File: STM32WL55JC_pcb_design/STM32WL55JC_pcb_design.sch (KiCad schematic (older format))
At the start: 40 parts, among them J1 Conn_01x03, J10 Conn_01x01_Male, J11 Conn_02x02_Odd_Even, J2 Conn_01x03, J3 Conn_02x05_Odd_Even, J4 Conn_01x03, J5 Conn_01x09, J6 Conn_01x09, J7 Conn_01x03, J8 Conn_01x09, J9 Conn_01x09, U1 STM32WL55JCI7, Y1 32MHz, Y2 32.768kHz

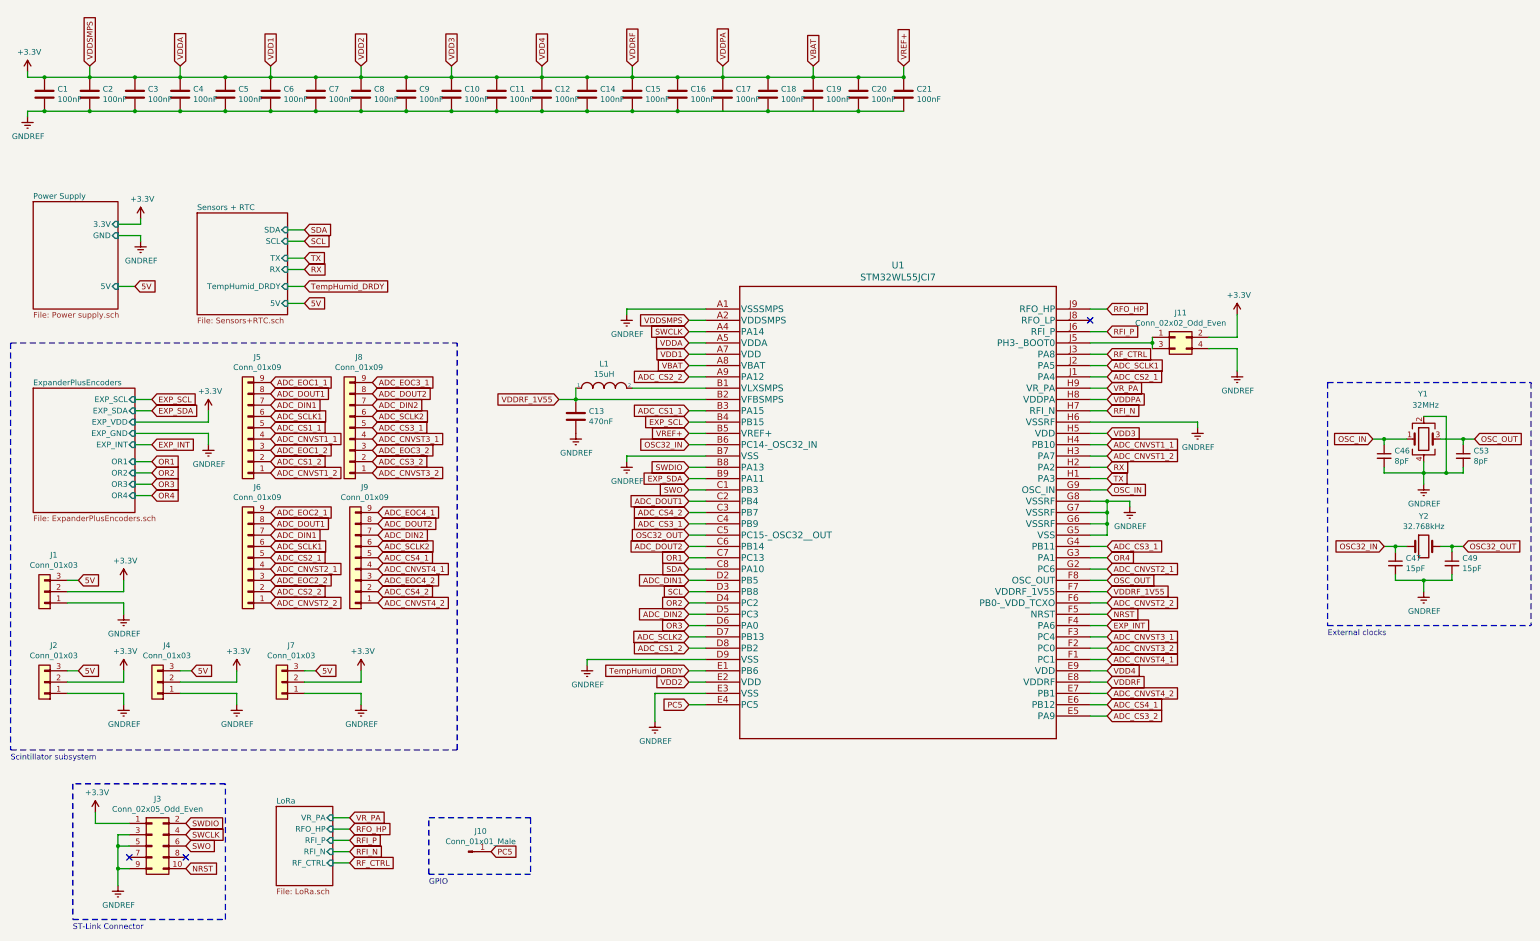
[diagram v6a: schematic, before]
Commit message: Initial pcb layout
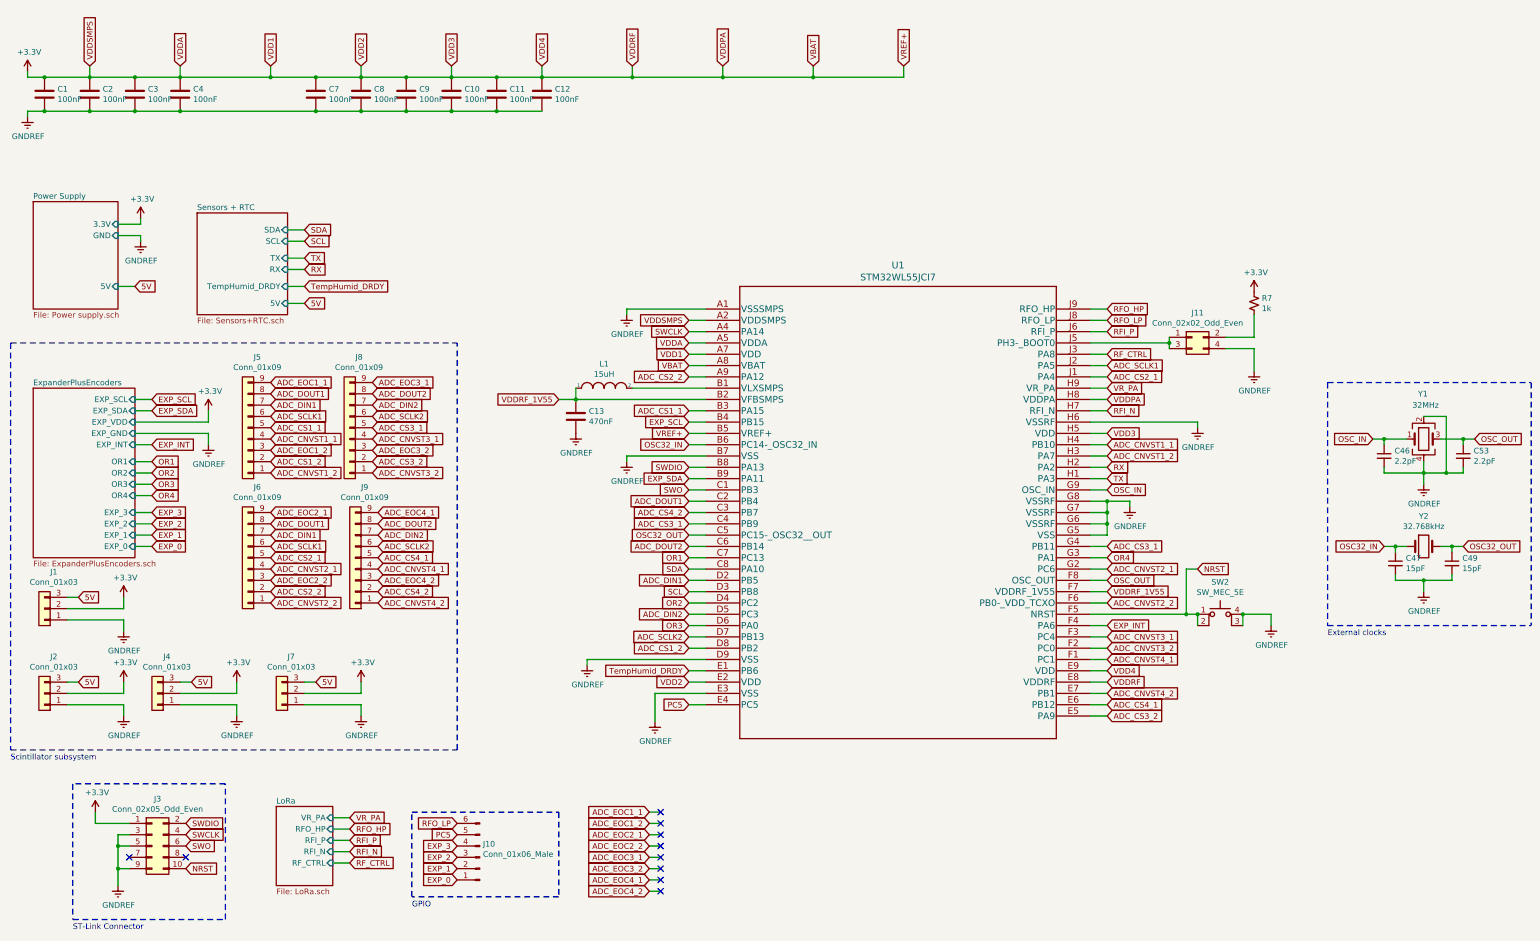
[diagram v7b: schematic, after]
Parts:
- removed C14, C15, C16, C17, C18, C19, C20, C21, C5, C6: 100nF, Capacitor_SMD:C_0805_2012Metric, symbol Device:C
- removed J10: Conn_01x01_Male, Connector_PinHeader_2.54mm:PinHeader_1x01_P2.54mm_Vertical, symbol Connector:Conn_01x01_Male
- added J10: Conn_01x06_Male, Connector_PinHeader_2.54mm:PinHeader_1x06_P2.54mm_Vertical, symbol Connector:Conn_01x06_Male
- added R7: 1k, Resistor_SMD:R_0805_2012Metric, symbol Device:R_Small_US
- added SW2: SW_MEC_5E, EVQ-P2F02K:EVQP2V02W, symbol Switch:SW_MEC_5E
- C46, C53: value 8pF -> 2.2pF
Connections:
- net +3V3: now also R7.1; no longer J11.2 (Pin_2)
- net GNDREF: now also SW2.3 (K), SW2.4 (A)
- net NRST: now also SW2.1, SW2.2
- net PC5: now also J10.5 (Pin_5)
- net RFO_LP: now reaches U1.J8 (RFO_LP)
- net RFO_LP: now also J10.6 (Pin_6)
- new net: J11.2 (Pin_2), R7.2
- new net EXP_0: J10.1 (Pin_1)
- new net EXP_1: J10.2 (Pin_2)
- new net EXP_2: J10.3 (Pin_3)
- new net EXP_3: J10.4 (Pin_4)
- no-connect marks 3 -> 10
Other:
- moved on the sheet: J1, J11, J2, J4, J7

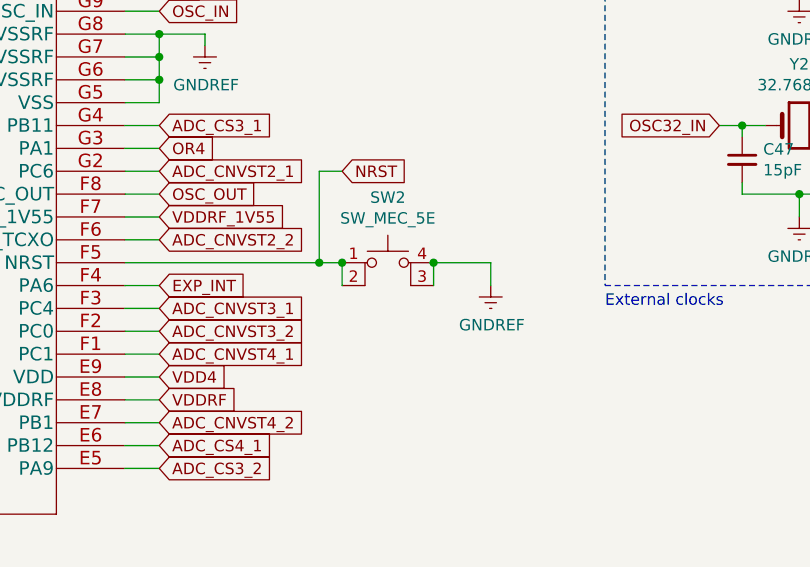
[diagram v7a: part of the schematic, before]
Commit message: Finished component placement
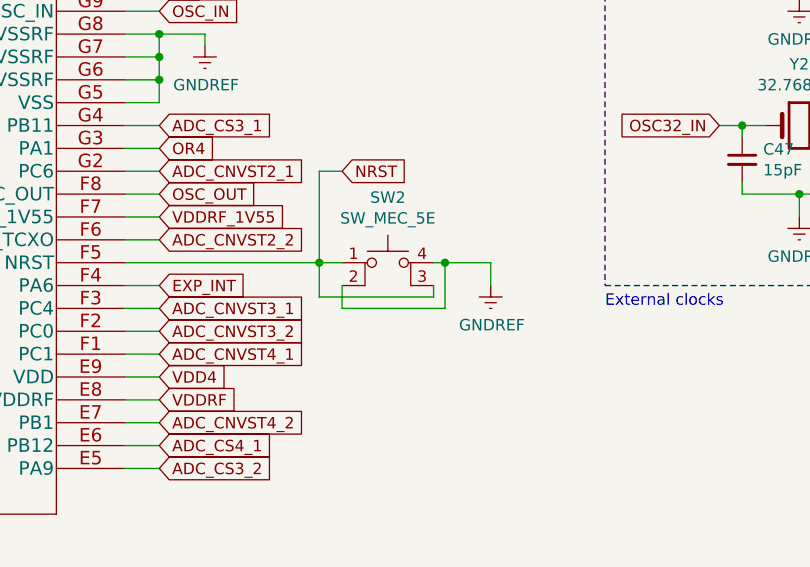
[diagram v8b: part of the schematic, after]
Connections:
- net GNDREF: now also SW2.2; no longer SW2.3 (K)
- net NRST: now also SW2.3 (K); no longer SW2.2
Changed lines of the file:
@@
 $EndComp
 Wire Wire Line
-	11450 5750 11700 5750
-Wire Wire Line
-	11050 5750 11050 5850
-Connection ~ 11050 5750
-Wire Wire Line
-	11450 5750 11450 5850
-Connection ~ 11450 5750
+	11450 5750 11500 5750
 Wire Wire Line
 	10950 5750 10950 5350
@@
 Wire Wire Line
 	6050 1000 6850 1000
+Wire Wire Line
+	11050 5850 11050 5950
+Wire Wire Line
+	11050 5950 11500 5950
+Wire Wire Line
+	11500 5950 11500 5750
+Connection ~ 11500 5750
+Wire Wire Line
+	11500 5750 11700 5750
+Wire Wire Line
+	10950 5750 10950 5900
+Wire Wire Line
+	10950 5900 11450 5900
+Wire Wire Line
+	11450 5900 11450 5850
 $EndSCHEMATC
